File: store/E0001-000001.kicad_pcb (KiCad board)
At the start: 2 copper layers, 104.9 x 47 mm, 44 parts, among them J1 Connector, J2 Connector, J3 WeAct_1, J4 WeAct_2, J5 Seansor_Header_A, J6 Seansor_Header_B, U1 TPS54302, U2 SN65HVD230, U3 ATECC608B-SSHDA

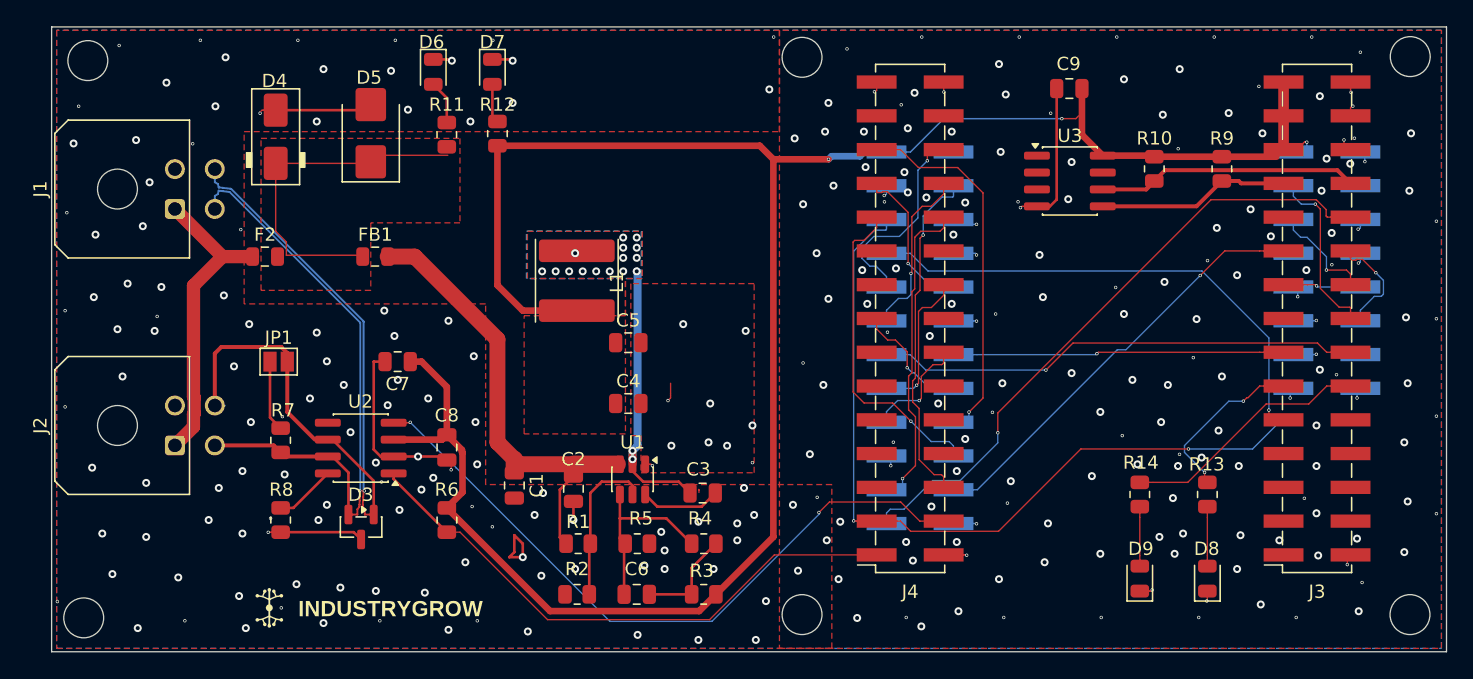
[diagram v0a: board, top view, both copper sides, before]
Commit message: Update PCB layout, DRC rules, and fab outputs
- kicad_pcb: layout rework
- kicad_pro: tighten min track width to 0.1017mm; widen microvia diameter to 0.6mm / drill to 0.3mm
- D-pos.csv: reposition D3
- L.csv: update R4 LCSC part to C149504
- gitignore KiCad local-history backup folder (store/.history/)

Signed-off-by: IIchukissII <133657307+IIchukissII@users.noreply.github.com>
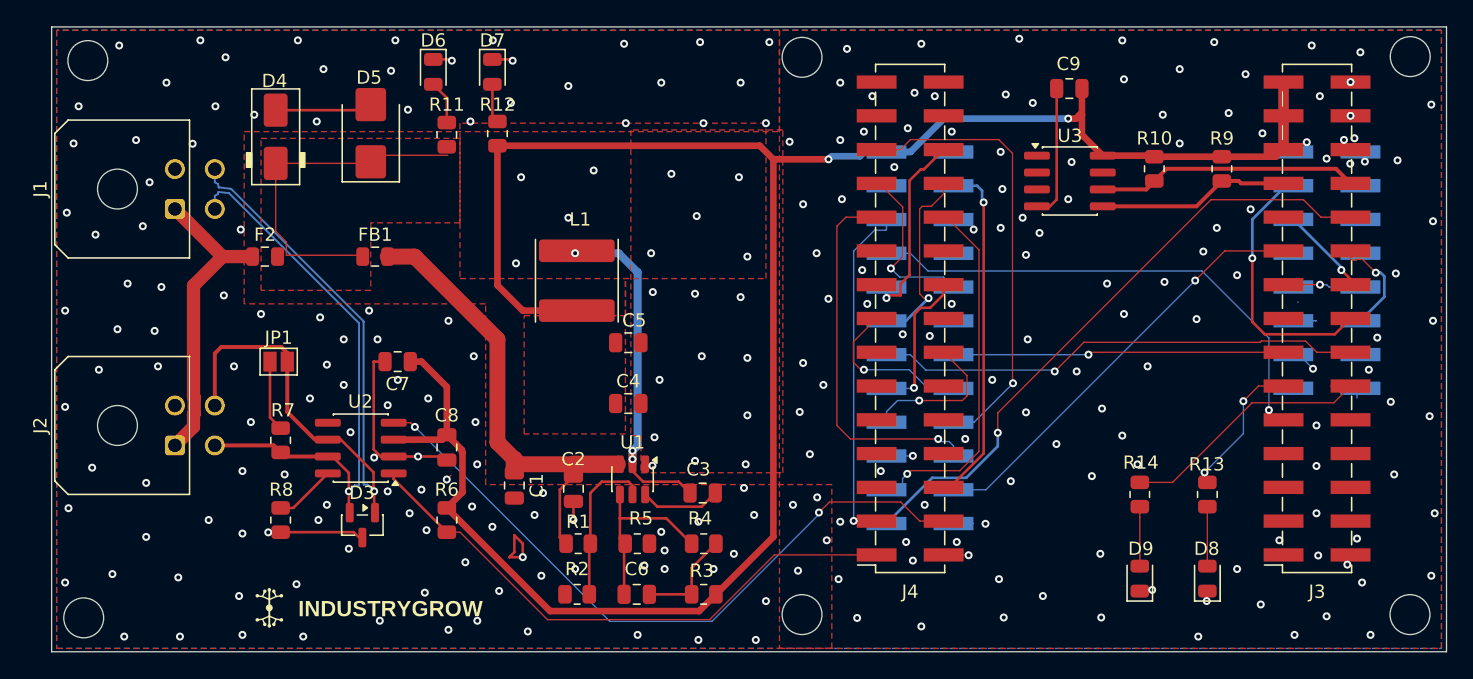
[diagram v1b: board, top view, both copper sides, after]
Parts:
- moved D3 0.17 mm to (80.6, 58.3)
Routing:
- net I2C1_SDA: track 62.6 -> 27.2 mm, vias 2 -> 1
- net GND: track 83.5 -> 67.8 mm, vias 293 -> 264
- net STRAP_0: track 12.9 -> 20.1 mm
- net GPIO_4: track 28.2 -> 33.9 mm
- net Net-(U1-SW): track 20.8 -> 26.0 mm, vias 17 -> 3
- net PWM_1: track 24.3 -> 28.9 mm
- net GPIO_3: track 8.38 -> 12.1 mm
- net USART1_RX: track 9.12 -> 12.4 mm
- net PWM_2: track 24.3 -> 27.3 mm
- net CAN_L: track 58.0 -> 55.5 mm
- net CAN_H: track 45.6 -> 43.1 mm
- net LED_CAN: track 12.9 -> 11.0 mm
- net LED_Status: track 18.9 -> 20.4 mm
- net SPI2_SCK: track 15.8 -> 14.4 mm
- net SPI2_MOSI: track 14.2 -> 15.5 mm
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- removed copper zone on B.Cu, net Net-(U1-SW)
- removed copper zone on F.Cu, net Net-(U1-SW)
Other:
- board text added: "E0001 V00.00.01"
- board text removed: "E0001 V0.0.01"

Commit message: feat(identifiers): add SP-number scheme, registry, and renumber M05-SAFETY
Introduce ADR-0019 (purchased-part SP-number identification) and a
top-level REGISTRY.md mapping E-numbers and SP-numbers to meaning. Renumber
the M05-SAFETY board from E0002 to E0006 so M01-M05 occupy E0002-E0006 in
taxonomy order, and reconcile ADR-0017 to the resolved deferred items.

- ADR-0017: drop duplicated invariant paragraph; condense decision 15 and
  alternative D; record WeAct as an SP part (ADR-0019); resolve the
  registry/store-location deferred item.
- REGISTRY.md: authoritative E-number / SP-number type registry.
- store: rename E0002-000001.* -> E0006-000001.* (KiCad project, render,
  internal sheet/project refs, and silk legend) for the M05-SAFETY design.
- store: carrier E0001 silk-layer fix (F.Paste -> F.SilkS).

Signed-off-by: IIchukissII <133657307+IIchukissII@users.noreply.github.com>
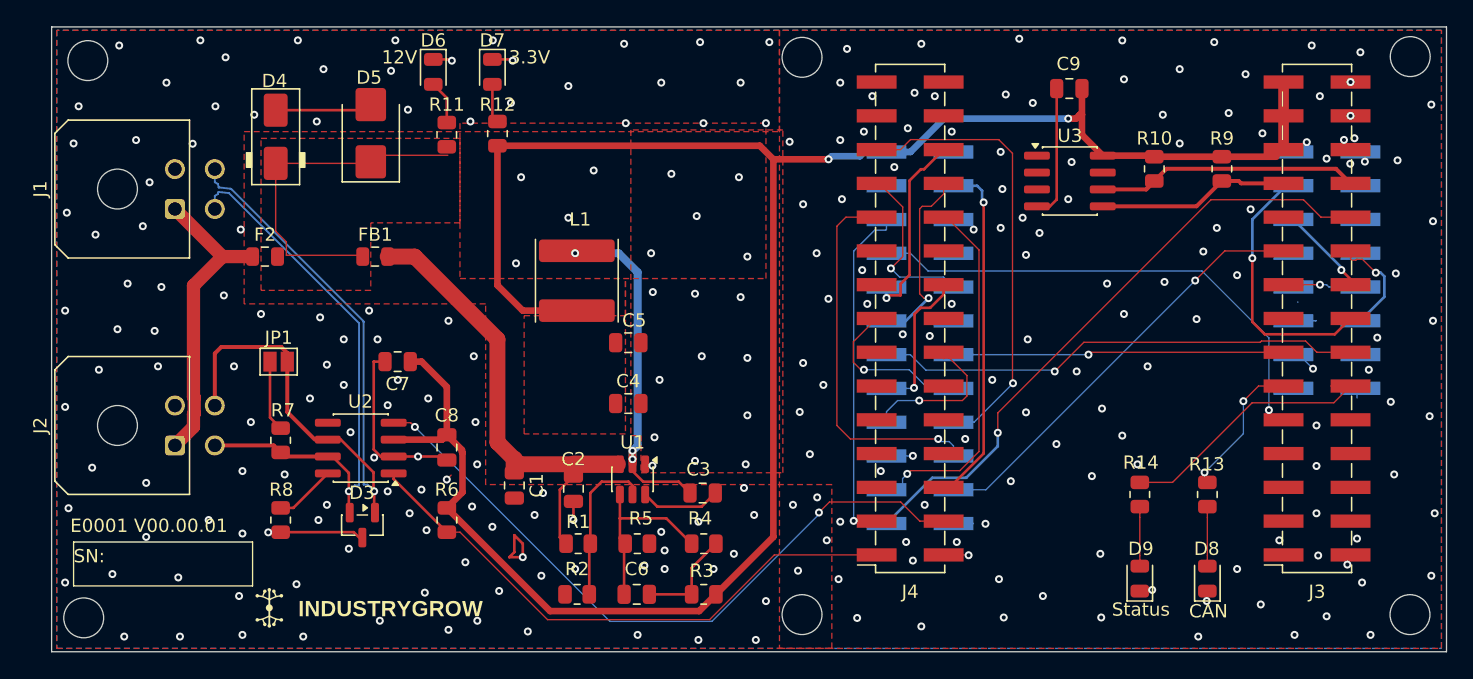
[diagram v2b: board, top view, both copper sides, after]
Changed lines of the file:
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@@
 		(capping no)
 		(filling no)
-		(zone_defaults)
 		(pcbplotparams
 			(layerselection 0x00000000_00000000_55555555_5755f5ff)
@@
 		(property "Value" "12V"
 			(at -1.0945 2.54 180)
-			(layer "F.Paste")
+			(layer "F.SilkS")
 			(effects
 				(font
@@
 		(property "Value" "3.3V"
 			(at -1.0945 -2.794 180)
-			(layer "F.Paste")
+			(layer "F.SilkS")
 			(effects
 				(font
@@
 		(property "Value" "Status"
 			(at -2.3265 0.079 180)
-			(layer "F.Paste")
+			(layer "F.SilkS")
 			(effects
 				(font
@@
 		(property "Value" "CAN"
 			(at -2.4535 0.079 180)
-			(layer "F.Paste")
+			(layer "F.SilkS")
 			(effects
 				(font
@@
 		(stroke
 			(width 0.1)
-			(type default)
+			(type solid)
 		)
 		(fill no)
-		(layer "F.Paste")
+		(layer "F.SilkS")
 	)
 	(gr_rect
@@
 	(gr_text "E0001 V00.00.01"
 		(at 58.674 58.928 0)
-		(layer "F.Paste")
+		(layer "F.SilkS")
 		(effects
 			(font
@@
 	(gr_text "SN:"
 		(at 58.928 61.214 0)
-		(layer "F.Paste")
+		(layer "F.SilkS")
 		(effects
 			(font
@@
 	)
 	(group ""
-		(members "b375398e-b063-4546-92b1-ea3762ec5c93" "b4ca4283-0706-4bb7-909c-d49c2ba8157e"
-			"d6ba6a0a-6e70-4cff-84a8-853f3f0ae174" "d8bde886-72a5-4905-9790-f0471499868d"
-			"dfc9826f-334d-4236-b197-fd21b09cc350" "ecee52fe-dd7b-4b77-bd17-10e43acd7cac"
+		(members "b375398e-b063-4546-92b1-ea3762ec5c93" "d6ba6a0a-6e70-4cff-84a8-853f3f0ae174"
+			"d8bde886-72a5-4905-9790-f0471499868d" "dfc9826f-334d-4236-b197-fd21b09cc350"
+			"ecee52fe-dd7b-4b77-bd17-10e43acd7cac"
 		)
 	)
